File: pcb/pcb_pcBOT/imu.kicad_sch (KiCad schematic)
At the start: 3 parts, among them U601 LSM6DSM

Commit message: pcb
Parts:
- added R1, R2: R_Small, symbol Device:R_Small
- C1: renamed from C602; value C_Small -> ~
- C2: renamed from C601; value C_Small -> ~
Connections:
- net GND: now also C1.2, C2.2, U601. (NC)
- net VDD: now also C1.1, U601.8 (VDD)
- net PB6: now reaches U601. (NC)
- net PB6: now also R1.2
- net PB7: now reaches U601.14 (SDA)
- net PB7: now also R2.2
- net VDDIO: now reaches U601.5 (VDDIO)
- net VDDIO: now also C2.1

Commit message: avancement des schematics
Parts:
- removed R1, R2: R_Small, symbol Device:R_Small
- C601: renamed from C2; value ~ -> 100n
- C602: renamed from C1; value ~ -> 100n
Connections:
- net PB6 is gone; now on net I2C_SCL: U601. (NC)
- net GND: now also U601.1 (SDO/SA0), U601.7 (GND)
- net VDD: now also U601.12 (CS)
- net I2C_SCL: now reaches U601. (NC)
- net IMU_INT1: now reaches U601.4 (INT1)
- net PB7 renamed I2C_SDA
- no-connect marks 0 -> 3
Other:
- note added: "Adresse : 0x6A (imposée)"
- note added: "I2C enable"
- note added: "Pull up déja présent sur bms (sheet 2)"
- company: (none) -> ENSEA G5
- title: (none) -> Imu PcBot

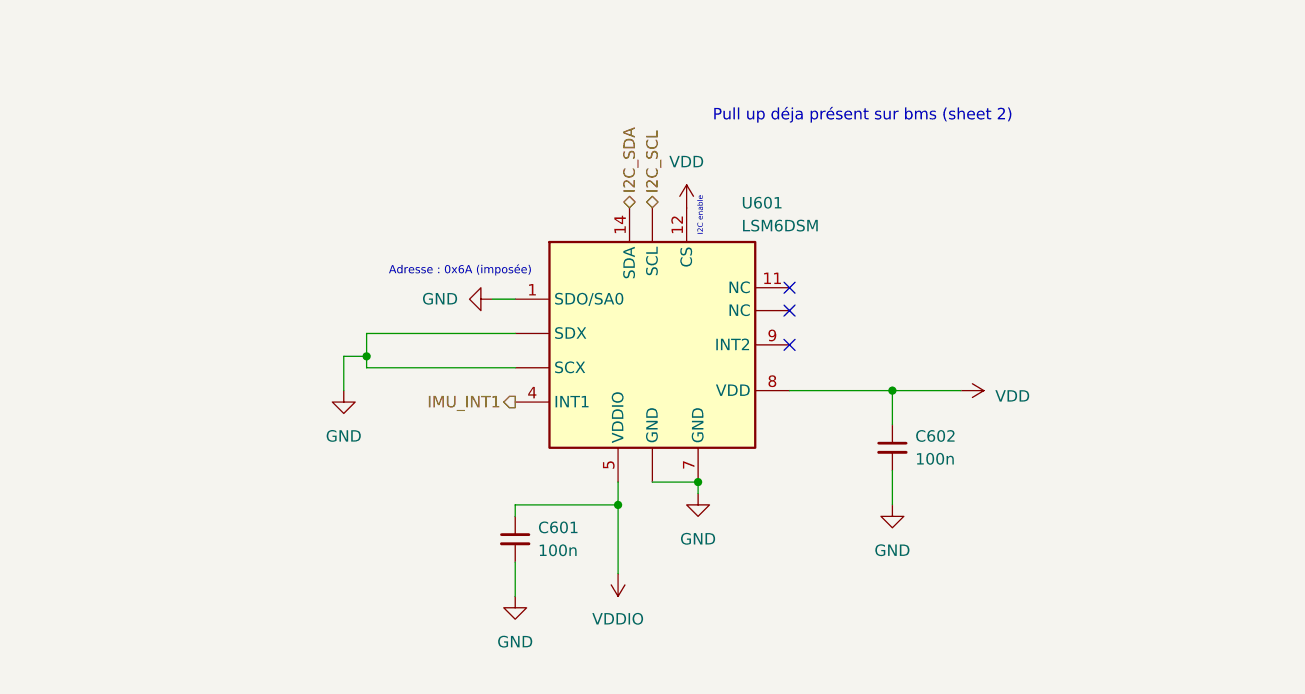
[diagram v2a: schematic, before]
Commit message: Ajout empreintes (incomplet) + test erc correct
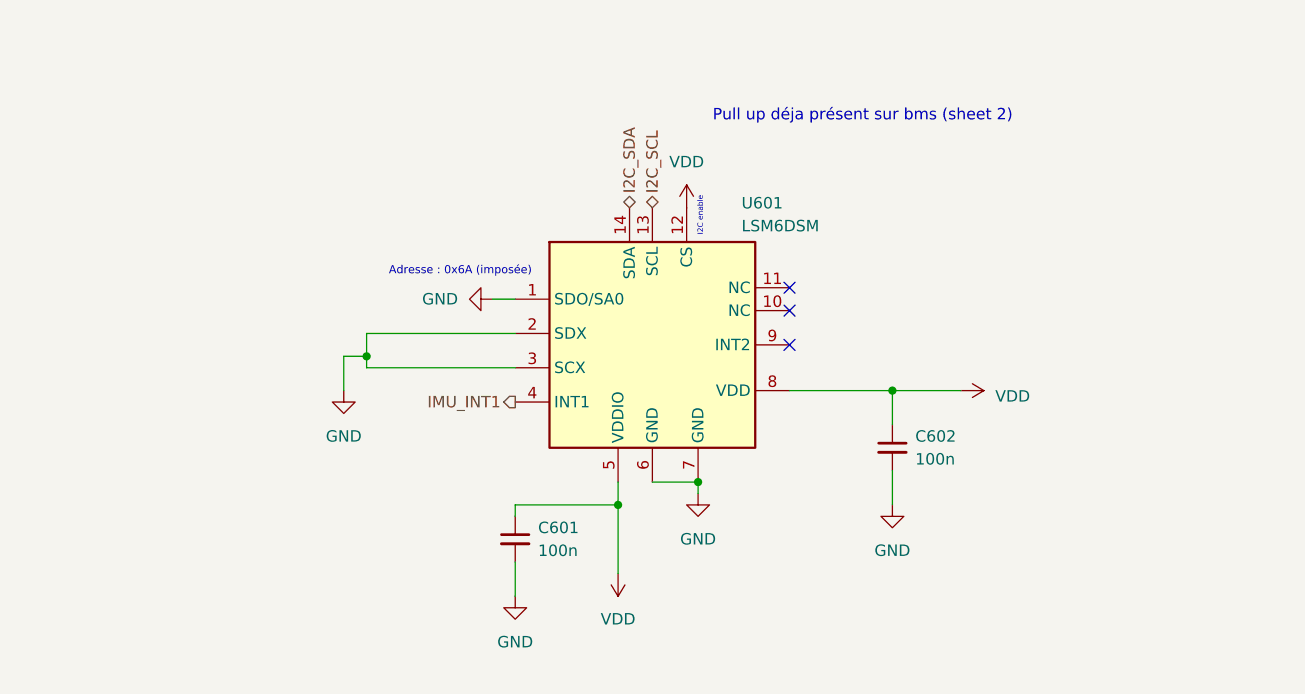
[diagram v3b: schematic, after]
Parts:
- C601, C602: footprint (none) -> Capacitor_SMD:C_0805_2012Metric_Pad1.18x1.45mm_HandSolder
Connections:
- net VDDIO is gone; now on net VDD: C601.1, U601.5 (VDDIO)
- net GND: now also U601.2 (SDX), U601.3 (SCX), U601.6 (GND); no longer U601. (NC)
- net I2C_SCL: now also U601.13 (SCL); no longer U601. (NC)
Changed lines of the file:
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@@
+	(symbol
+		(lib_id "power:VDD")
+		(at 151.13 104.14 180)
+		(unit 1)
+		(exclude_from_sim no)
+		(in_bom yes)
+		(on_board yes)
+		(dnp no)
+		(fields_autoplaced yes)
+		(property "Reference" "#PWR0603"
+			(at 151.13 100.33 0)
+			(effects
+				(font
+					(size 1.27 1.27)
+				)
+				(hide yes)
+			)
+		)
+		(property "Value" "VDD"
+			(at 151.13 109.22 0)
+			(effects
+				(font
+					(size 1.27 1.27)
+				)
+			)
+		)
+		(property "Footprint" ""
+			(at 151.13 104.14 0)
+			(effects
+				(font
+					(size 1.27 1.27)
+				)
+				(hide yes)
+			)
+		)
+		(property "Datasheet" ""
+			(at 151.13 104.14 0)
+			(effects
+				(font
+					(size 1.27 1.27)
+				)
+				(hide yes)
+			)
+		)
+		(property "Description" "Power symbol creates a global label with name \"VDD\""
+			(at 151.13 104.14 0)
+			(effects
+				(font
+					(size 1.27 1.27)
+				)
+				(hide yes)
+			)
+		)
+		(pin "1"
+		)
+		(instances
+			(project ""
+				(path "/704e4da3-8ee7-458f-8a0f-3fc97e8dc2a6/ccd57063-24ab-4973-bd12-151ee600ad9c"
+					(reference "#PWR0603")
+					(unit 1)
+				)
+			)
+		)
+	)
 	(symbol
 		(lib_id "power:VDD")
@@
 	)
 	(symbol
-		(lib_id "power:VCC")
-		(at 151.13 104.14 180)
-		(unit 1)
-		(exclude_from_sim no)
-		(in_bom yes)
-		(on_board yes)
-		(dnp no)
-		(fields_autoplaced yes)
-		(property "Reference" "#PWR0603"
-			(at 151.13 100.33 0)
-			(effects
-				(font
-					(size 1.27 1.27)
-				)
-				(hide yes)
-			)
-		)
-		(property "Value" "VDDIO"
-			(at 151.13 109.22 0)
-			(effects
-				(font
-					(size 1.27 1.27)
-				)
-			)
-		)
-		(property "Footprint" ""
-			(at 151.13 104.14 0)
-			(effects
-				(font
-					(size 1.27 1.27)
-				)
-				(hide yes)
-			)
-		)
-		(property "Datasheet" ""
-			(at 151.13 104.14 0)
-			(effects
-				(font
-					(size 1.27 1.27)
-				)
-				(hide yes)
-			)
-		)
-		(property "Description" "Power symbol creates a global label with name \"VCC\""
-			(at 151.13 104.14 0)
-			(effects
-				(font
-					(size 1.27 1.27)
-				)
-				(hide yes)
-			)
-		)
-		(pin "1"
-		)
-		(instances
-			(project ""
-				(path "/704e4da3-8ee7-458f-8a0f-3fc97e8dc2a6/ccd57063-24ab-4973-bd12-151ee600ad9c"
-					(reference "#PWR0603")
-					(unit 1)
-				)
-			)
-		)
-	)
-	(symbol
 		(lib_id "power:GND")
 		(at 139.7 106.68 0)
@@
 		(pin "9"
 		)
-		(pin ""
-		)
-		(pin ""
-		)
-		(pin ""
-		)
-		(pin ""
-		)
-		(pin ""
+		(pin "3"
+		)
+		(pin "10"
+		)
+		(pin "2"
+		)
+		(pin "6"
+		)
+		(pin "13"
 		)
 		(instances
@@
 			)
 		)
-		(property "Footprint" ""
+		(property "Footprint" "Capacitor_SMD:C_0805_2012Metric_Pad1.18x1.45mm_HandSolder"
 			(at 181.61 90.17 0)
 			(effects
@@
 			)
 		)
-		(property "Footprint" ""
+		(property "Footprint" "Capacitor_SMD:C_0805_2012Metric_Pad1.18x1.45mm_HandSolder"
 			(at 139.7 100.33 0)
 			(effects

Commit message: Revert "Ajout empreintes (incomplet) + test erc correct"
This reverts commit 267ed5519d67c336b99c9c80b0ac2067182b82a3.
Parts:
- C601, C602: footprint Capacitor_SMD:C_0805_2012Metric_Pad1.18x1.45mm_HandSolder -> (none)
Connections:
- net GND: now also U601. (NC); no longer U601.2 (SDX), U601.3 (SCX), U601.6 (GND)
- net I2C_SCL: now also U601. (NC); no longer U601.13 (SCL)
- net VDD: no longer C601.1, U601.5 (VDDIO)
- new net VDDIO: C601.1, U601.5 (VDDIO)
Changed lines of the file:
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@@
 	(symbol
 		(lib_id "power:VDD")
+		(at 189.23 83.82 270)
+		(unit 1)
+		(exclude_from_sim no)
+		(in_bom yes)
+		(on_board yes)
+		(dnp no)
+		(fields_autoplaced yes)
+		(property "Reference" "#PWR0605"
+			(at 185.42 83.82 0)
+			(effects
+				(font
+					(size 1.27 1.27)
+				)
+				(hide yes)
+			)
+		)
+		(property "Value" "VDD"
+			(at 193.04 84.455 90)
+			(effects
+				(font
+					(size 1.27 1.27)
+				)
+				(justify left)
+			)
+		)
+		(property "Footprint" ""
+			(at 189.23 83.82 0)
+			(effects
+				(font
+					(size 1.27 1.27)
+				)
+				(hide yes)
+			)
+		)
+		(property "Datasheet" ""
+			(at 189.23 83.82 0)
+			(effects
+				(font
+					(size 1.27 1.27)
+				)
+				(hide yes)
+			)
+		)
+		(property "Description" "Power symbol creates a global label with name \"VDD\""
+			(at 189.23 83.82 0)
+			(effects
+				(font
+					(size 1.27 1.27)
+				)
+				(hide yes)
+			)
+		)
+		(pin "1"
+		)
+		(instances
+			(project "pcb_pcBOT"
+				(path "/704e4da3-8ee7-458f-8a0f-3fc97e8dc2a6/ccd57063-24ab-4973-bd12-151ee600ad9c"
+					(reference "#PWR0605")
+					(unit 1)
+				)
+			)
+		)
+	)
+	(symbol
+		(lib_id "power:GND")
+		(at 137.16 73.66 270)
+		(unit 1)
+		(exclude_from_sim no)
+		(in_bom yes)
+		(on_board yes)
+		(dnp no)
+		(fields_autoplaced yes)
+		(property "Reference" "#PWR0607"
+			(at 130.81 73.66 0)
+			(effects
+				(font
+					(size 1.27 1.27)
+				)
+				(hide yes)
+			)
+		)
+		(property "Value" "GND"
+			(at 133.35 73.6599 90)
+			(effects
+				(font
+					(size 1.27 1.27)
+				)
+				(justify right)
+			)
+		)
+		(property "Footprint" ""
+			(at 137.16 73.66 0)
+			(effects
+				(font
+					(size 1.27 1.27)
+				)
+				(hide yes)
+			)
+		)
+		(property "Datasheet" ""
+			(at 137.16 73.66 0)
+			(effects
+				(font
+					(size 1.27 1.27)
+				)
+				(hide yes)
+			)
+		)
+		(property "Description" "Power symbol creates a global label with name \"GND\" , ground"
+			(at 137.16 73.66 0)
+			(effects
+				(font
+					(size 1.27 1.27)
+				)
+				(hide yes)
+			)
+		)
+		(pin "1"
+		)
+		(instances
+			(project ""
+				(path "/704e4da3-8ee7-458f-8a0f-3fc97e8dc2a6/ccd57063-24ab-4973-bd12-151ee600ad9c"
+					(reference "#PWR0607")
+					(unit 1)
+				)
+			)
+		)
+	)
+	(symbol
+		(lib_id "power:VCC")
 		(at 151.13 104.14 180)
 		(unit 1)
@@
 			)
 		)
-		(property "Value" "VDD"
+		(property "Value" "VDDIO"
 			(at 151.13 109.22 0)
 			(effects
@@
 			)
 		)
-		(property "Description" "Power symbol creates a global label with name \"VDD\""
+		(property "Description" "Power symbol creates a global label with name \"VCC\""
 			(at 151.13 104.14 0)
 			(effects
@@
 				(path "/704e4da3-8ee7-458f-8a0f-3fc97e8dc2a6/ccd57063-24ab-4973-bd12-151ee600ad9c"
 					(reference "#PWR0603")
-					(unit 1)
-				)
-			)
-		)
-	)
-	(symbol
-		(lib_id "power:VDD")
-		(at 189.23 83.82 270)
-		(unit 1)
-		(exclude_from_sim no)
-		(in_bom yes)
-		(on_board yes)
-		(dnp no)
-		(fields_autoplaced yes)
-		(property "Reference" "#PWR0605"
-			(at 185.42 83.82 0)
-			(effects
-				(font
-					(size 1.27 1.27)
-				)
-				(hide yes)
-			)
-		)
-		(property "Value" "VDD"
-			(at 193.04 84.455 90)
-			(effects
-				(font
-					(size 1.27 1.27)
-				)
-				(justify left)
-			)
-		)
-		(property "Footprint" ""
-			(at 189.23 83.82 0)
-			(effects
-				(font
-					(size 1.27 1.27)
-				)
-				(hide yes)
-			)
-		)
-		(property "Datasheet" ""
-			(at 189.23 83.82 0)
-			(effects
-				(font
-					(size 1.27 1.27)
-				)
-				(hide yes)
-			)
-		)
-		(property "Description" "Power symbol creates a global label with name \"VDD\""
-			(at 189.23 83.82 0)
-			(effects
-				(font
-					(size 1.27 1.27)
-				)
-				(hide yes)
-			)
-		)
-		(pin "1"
-		)
-		(instances
-			(project "pcb_pcBOT"
-				(path "/704e4da3-8ee7-458f-8a0f-3fc97e8dc2a6/ccd57063-24ab-4973-bd12-151ee600ad9c"
-					(reference "#PWR0605")
-					(unit 1)
-				)
-			)
-		)
-	)
-	(symbol
-		(lib_id "power:GND")
-		(at 137.16 73.66 270)
-		(unit 1)
-		(exclude_from_sim no)
-		(in_bom yes)
-		(on_board yes)
-		(dnp no)
-		(fields_autoplaced yes)
-		(property "Reference" "#PWR0607"
-			(at 130.81 73.66 0)
-			(effects
-				(font
-					(size 1.27 1.27)
-				)
-				(hide yes)
-			)
-		)
-		(property "Value" "GND"
-			(at 133.35 73.6599 90)
-			(effects
-				(font
-					(size 1.27 1.27)
-				)
-				(justify right)
-			)
-		)
-		(property "Footprint" ""
-			(at 137.16 73.66 0)
-			(effects
-				(font
-					(size 1.27 1.27)
-				)
-				(hide yes)
-			)
-		)
-		(property "Datasheet" ""
-			(at 137.16 73.66 0)
-			(effects
-				(font
-					(size 1.27 1.27)
-				)
-				(hide yes)
-			)
-		)
-		(property "Description" "Power symbol creates a global label with name \"GND\" , ground"
-			(at 137.16 73.66 0)
-			(effects
-				(font
-					(size 1.27 1.27)
-				)
-				(hide yes)
-			)
-		)
-		(pin "1"
-		)
-		(instances
-			(project ""
-				(path "/704e4da3-8ee7-458f-8a0f-3fc97e8dc2a6/ccd57063-24ab-4973-bd12-151ee600ad9c"
-					(reference "#PWR0607")
 					(unit 1)
 				)
@@
 		(pin "9"
 		)
-		(pin "3"
-		)
-		(pin "10"
-		)
-		(pin "2"
-		)
-		(pin "6"
-		)
-		(pin "13"
+		(pin ""
+		)
+		(pin ""
+		)
+		(pin ""
+		)
+		(pin ""
+		)
+		(pin ""
 		)
 		(instances
@@
 			)
 		)
-		(property "Footprint" "Capacitor_SMD:C_0805_2012Metric_Pad1.18x1.45mm_HandSolder"
+		(property "Footprint" ""
 			(at 181.61 90.17 0)
 			(effects
@@
 			)
 		)
-		(property "Footprint" "Capacitor_SMD:C_0805_2012Metric_Pad1.18x1.45mm_HandSolder"
+		(property "Footprint" ""
 			(at 139.7 100.33 0)
 			(effects
